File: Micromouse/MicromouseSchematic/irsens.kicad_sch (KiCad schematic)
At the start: 28 parts, among them J6 IR_1, J7 IR_2, J8 IR_3, J9 IR_4, Q1 SFH300, Q2 DMN3065LW-7, Q3 DMN3065LW-7, Q4 DMN3065LW-7, Q5 DMN3065LW-7, Q6 SFH300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

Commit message: Cleared all footprint errors and issues. Updated crystal caps to match Cload
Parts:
- J6, J7, J8, J9: footprint (none) -> Connector_JST:JST_ZH_B4B-ZR_1x04_P1.50mm_Vertical
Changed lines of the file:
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@@
 			)
 		)
-		(property "Footprint" ""
+		(property "Footprint" "Connector_JST:JST_ZH_B4B-ZR_1x04_P1.50mm_Vertical"
 			(at 139.7 55.88 0)
 			(effects
@@
 			)
 		)
-		(property "Footprint" ""
+		(property "Footprint" "Connector_JST:JST_ZH_B4B-ZR_1x04_P1.50mm_Vertical"
 			(at 140.97 109.22 0)
 			(effects
@@
 			)
 		)
-		(property "Footprint" ""
+		(property "Footprint" "Connector_JST:JST_ZH_B4B-ZR_1x04_P1.50mm_Vertical"
 			(at 46.99 109.22 0)
 			(effects
@@
 			)
 		)
-		(property "Footprint" ""
+		(property "Footprint" "Connector_JST:JST_ZH_B4B-ZR_1x04_P1.50mm_Vertical"
 			(at 43.18 55.88 0)
 			(effects

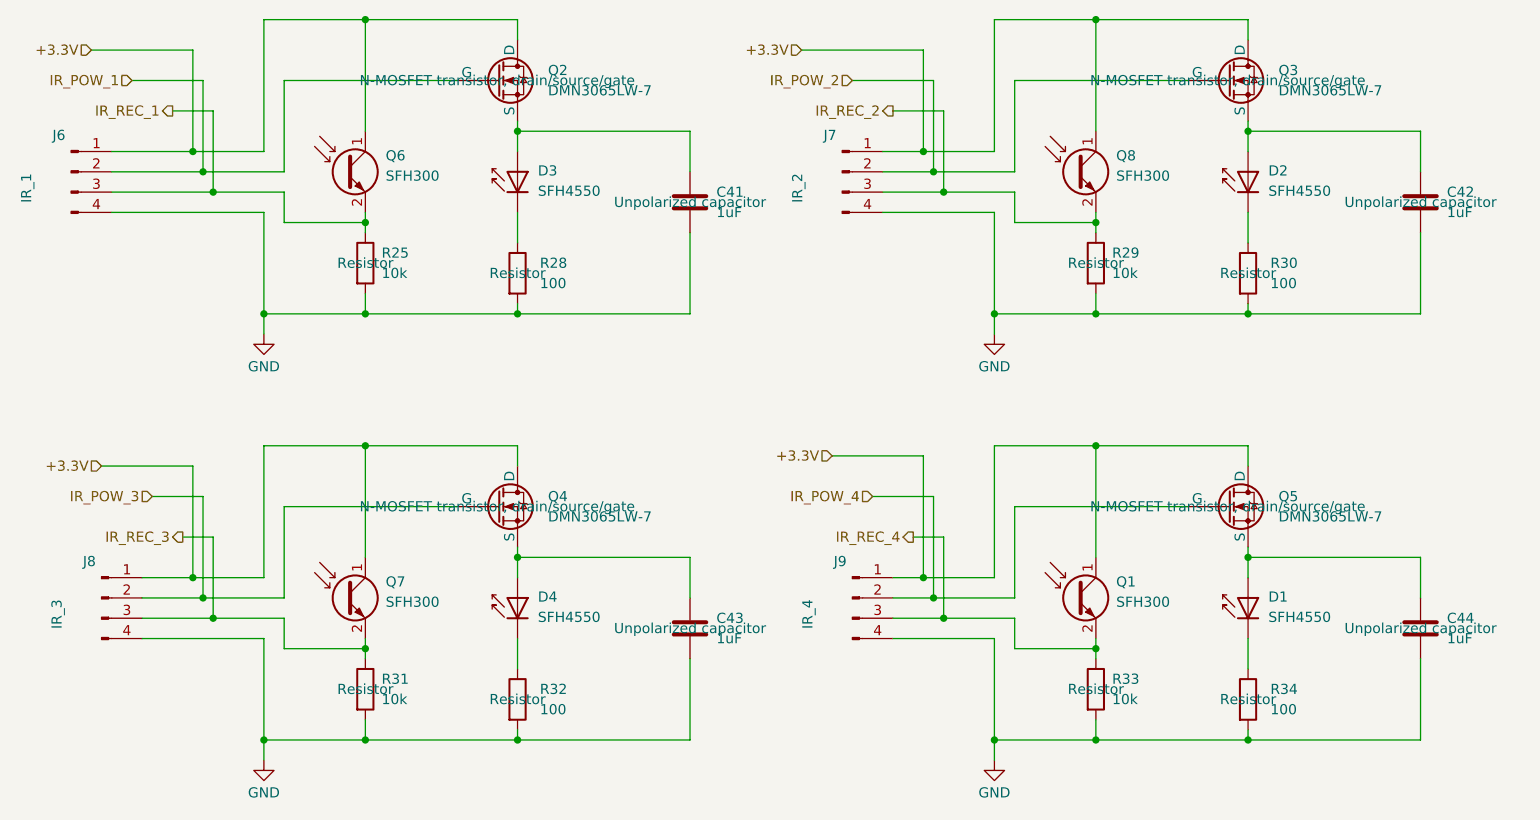
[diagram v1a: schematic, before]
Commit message: added ir sensors stuff
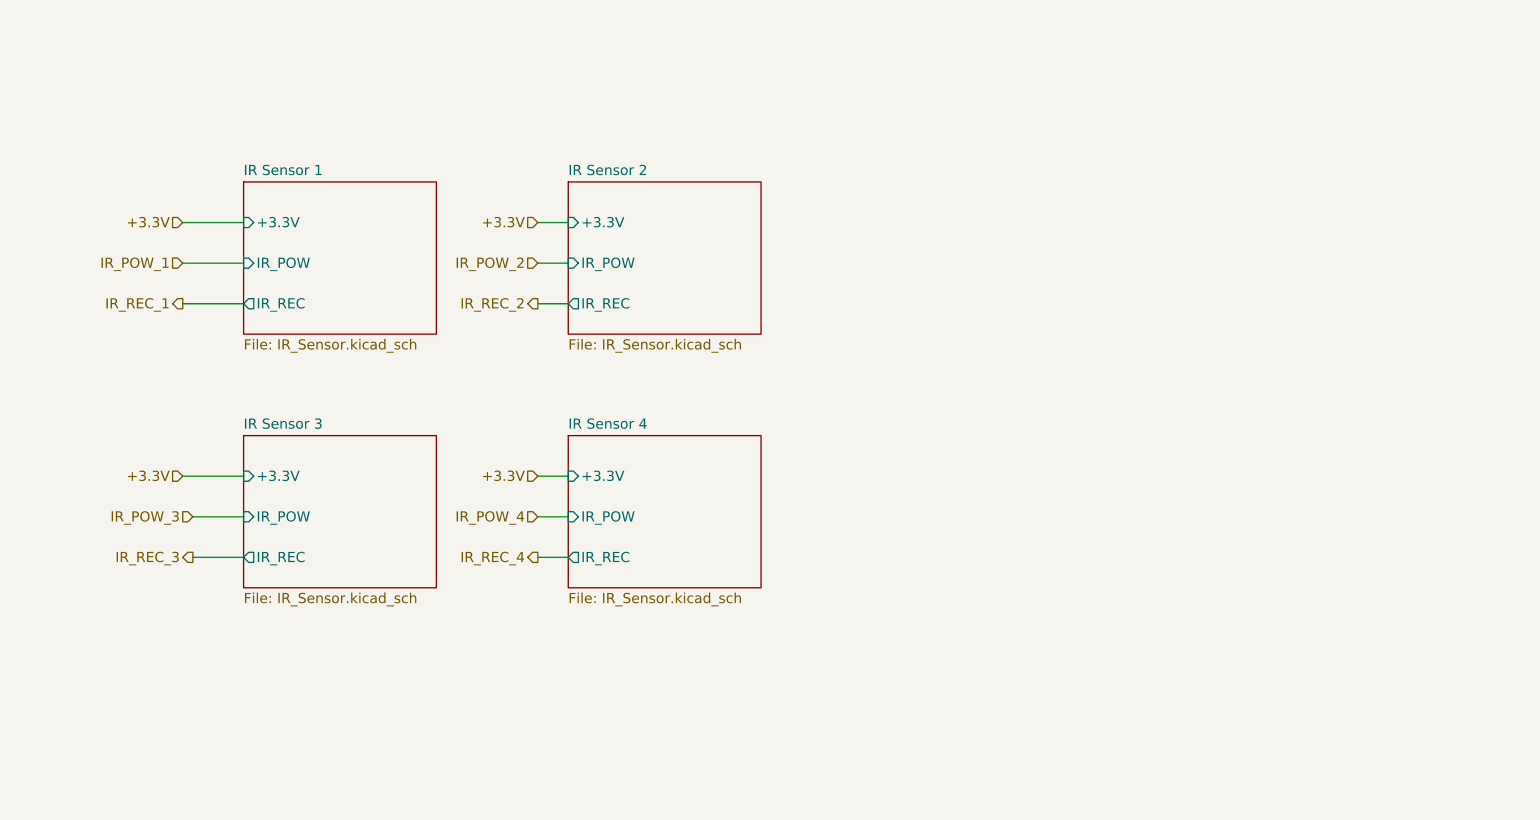
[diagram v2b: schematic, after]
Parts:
- removed C41, C42, C43, C44: 1uF, Capacitor_SMD:C_0402_1005Metric, symbol Device:C
- removed D1, D2, D3, D4: SFH4550, LED_THT:LED_D5.0mm_IRGrey, symbol LED:SFH4550
- removed J6: IR_1, Connector_JST:JST_ZH_B4B-ZR_1x04_P1.50mm_Vertical, symbol Connector:Conn_01x04_Pin
- removed J7: IR_2, Connector_JST:JST_ZH_B4B-ZR_1x04_P1.50mm_Vertical, symbol Connector:Conn_01x04_Pin
- removed J8: IR_3, Connector_JST:JST_ZH_B4B-ZR_1x04_P1.50mm_Vertical, symbol Connector:Conn_01x04_Pin
- removed J9: IR_4, Connector_JST:JST_ZH_B4B-ZR_1x04_P1.50mm_Vertical, symbol Connector:Conn_01x04_Pin
- removed Q1, Q6, Q7, Q8: SFH300, LED_THT:LED_D5.0mm_Clear, symbol Sensor_Optical:SFH300
- removed Q2, Q3, Q4, Q5: DMN3065LW-7, MM_DMN3065LW-7:DMN3065LW-7, symbol Simulation_SPICE:NMOS
- removed R25, R29, R31, R33: 10k, Resistor_SMD:R_0603_1608Metric, symbol Device:R
- removed R28, R30, R32, R34: 100, Resistor_SMD:R_0603_1608Metric, symbol Device:R
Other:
- added sheet IR Sensor 1 (IR_Sensor.kicad_sch)
- added sheet IR Sensor 2 (IR_Sensor.kicad_sch)
- added sheet IR Sensor 3 (IR_Sensor.kicad_sch)
- added sheet IR Sensor 4 (IR_Sensor.kicad_sch)
